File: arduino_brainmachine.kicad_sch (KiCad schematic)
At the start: 180 parts, among them Q1 2N5551, Q2 2N5551, Q3 2N5551, Q4 2N5551, Q5 BD139, Q6 BD139, Q8 2N5551, SW1 SW_Push, U1 TVS 05V, U2 TVS 05V, U3 LM358_DFN, U4 L7805_TO220, U5 TVS 12V, U6 TVS 12V, Y1 6.5 KHz or 2.5 kHz, Y2 6.5 KHz or 2.5 kHz, Y3 6.5 KHz or 2.5 kHz

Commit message: Upgrade
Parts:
- removed SW1: SW_Push, symbol Switch:SW_Push
- added C51, C52: 10-20, symbol Device:C_Small
- added D29, D30: D, symbol Device:D
- added D31, D32, D33, D34: LED, symbol Device:LED
- added Q7, Q9: 2N2222, Package_TO_SOT_THT:TO-39-3, symbol Transistor_BJT:2N2219
- added R60, R77: 10 KOm, symbol PCM_Elektuur:R
- added R61, R79: 100 KOm, symbol PCM_Elektuur:R
- added R75, R76, R78, R80, R81: 1 kOm, symbol PCM_Elektuur:R
- Q4, Q8: value 2N5551 -> 2N2222
- R21: value 220 Om -> 1 kOm
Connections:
- net +5V: now also R61.2 (-), R75.2 (-), R79.2 (-), R80.2 (-)
- net GND: now also C51.2, C52.2, D29.2 (A), D30.2 (A), D31.1 (K), D32.1 (K), D33.1 (K), D34.1 (K), Q7.1 (E), Q9.1 (E), R60.1 (+), R77.1 (+)
- net LED: now also A1.1 (D1/TX), A1.2 (D0/RX), R21.2 (-), R81.2 (-)
- net at D1.2 (A), D2.2 (A), R10.2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: now also D34.2 (A)
- net at D10.2 (A), D8.2 (A), R30.2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: now also D33.2 (A)
- net at R21.1 (+): now also D31.2 (A); no longer A1.5 (D2)
- net at D23.2 (A): now also C51.1, D29.1 (K), Q7.3 (C), R75.1 (+); no longer A1.10 (D7)
- net at A1.13 (D10): now also R76.2 (-); no longer D24.2 (A)
- new net: Q7.2 (B), R60.2 (-), R61.1 (+), R76.1 (+)
- new net: Q9.2 (B), R77.2 (-), R78.1 (+), R79.1 (+)
- new net: A1.10 (D7), R78.2 (-)
- new net: D32.2 (A), R81.1 (+)
- new net LEDPD: C52.1, D24.2 (A), D30.1 (K), Q9.3 (C), R80.1 (+)
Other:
- note removed: "Im dont use this switch and BrainWave Entertaiment program from spring"
- moved on the sheet: RV1, RV2, RV3, RV4

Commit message: Upgrade
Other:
- note added: "2025.09.03"
- note added: "Must be OSH"
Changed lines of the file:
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@@
 		(date "2025-02-18")
+	)
+	(text "2025.09.03"
+		(exclude_from_sim no)
+		(at 257.81 183.642 0)
+		(effects
+			(font
+				(size 1.27 1.27)
+			)
+		)
 	)
 	(text "Install all from first to bigger value"
@@
 		(effects
 			(font
+				(size 1.27 1.27)
+			)
+		)
+	)
+	(text "Must be OSH"
+		(exclude_from_sim no)
+		(at 254.508 177.8 0)
+		(effects
+			(font

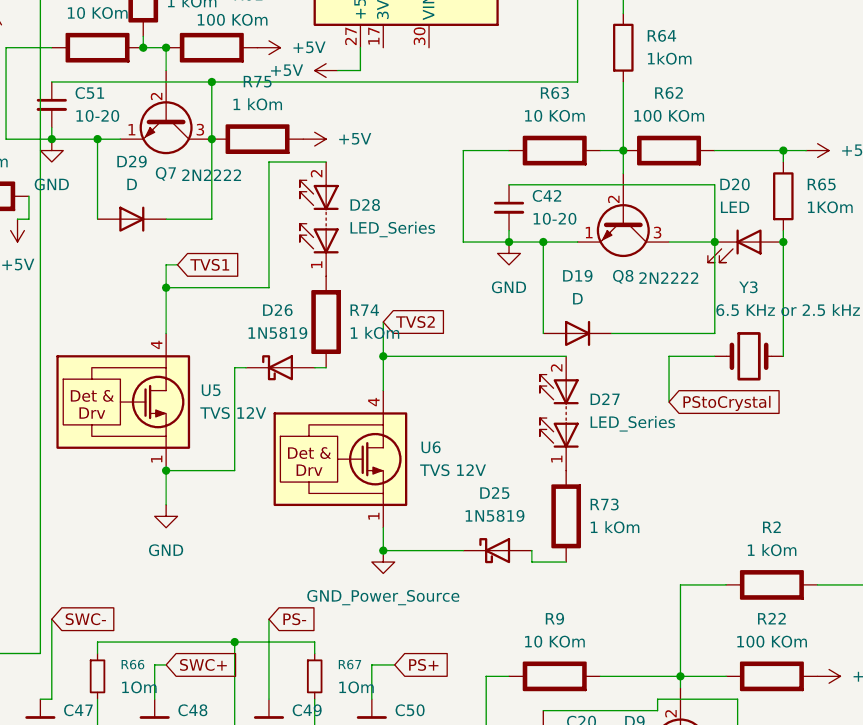
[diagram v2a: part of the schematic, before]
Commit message: Removed thing from piracy
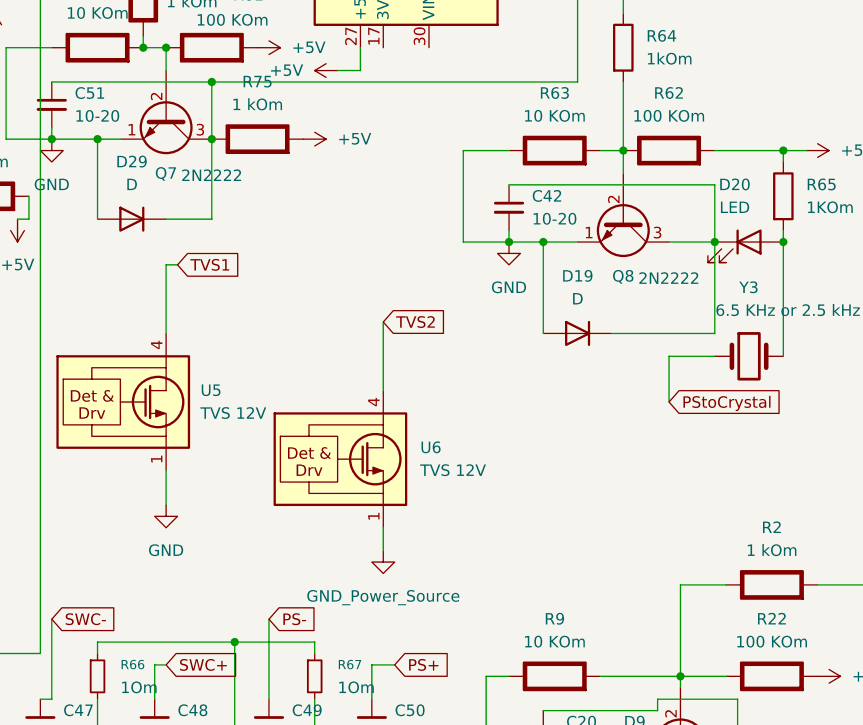
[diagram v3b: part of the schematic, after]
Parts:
- removed D25, D26: 1N5819, Diode_THT:D_DO-41_SOD81_P10.16mm_Horizontal, symbol Diode:1N5819
- removed D27, D28: LED_Series, symbol Device:LED_Series
- removed R73, R74: 1 kOm, symbol PCM_Elektuur:R

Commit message: Upgrade
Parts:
- removed C12, C14, C36, C37: 100nF, symbol PCM_Elektuur:C
- removed D23: LED, symbol Device:LED
- removed R59: 220 Om, symbol PCM_Elektuur:R
- removed R66, R67, R68, R69, R70: 1Om, symbol Device:R_Small
- added C12: 10-20, symbol Device:C_Small
- added D23: D, symbol Device:D
- added Q10: 2N2222, Package_TO_SOT_THT:TO-39-3, symbol Transistor_BJT:2N2219
- added Q11: BD139, Package_TO_SOT_THT:TO-39-3, symbol Transistor_BJT:2N2219
- added R59, R73, R74: 1KOm, symbol Device:R
- added U7, U8, U9: PC123, symbol Isolator:Optocoupler_DC_PhotoNPN_AKEC
- C19, C21, C24, C27, C39, C41: value 100pF-100nF -> 100pF-100nF and 100-1000nF
- D24: value LED -> 12v LED, 3-4 cm strip
- Q3: value 2N5551 -> 2N2222
- R37: value 220 Om -> 10 KOm
- R38: value 220 Om -> 100 KOm
- R58: value 220 Om -> 1 kOm
- renumbered C1 to C1?????, C2 to C2?????, C3 to C3????, C4 to C4?????
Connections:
- net +5V: now also R38.2 (-), U9.1
- net Earth_Protective: now also 12V.2 (A+), 5.1V.2 (A+), 5.1V1.2 (A+), A1.29 (GND), A1.4 (GND), C10.2 (-), C11.2 (-), C13.2 (-), C15.2 (-), C17.2 (-), C18.2 (-), C20.2, C23.2, C38.2 (-), C39.2, C40.2 (-), C41.2, C42.2, C43.1, C44.1, C45.1, C46.1, C47.2, C48.2, C49.2, C50.2, C51.2, C52.2, C7.2 (-), C9.2, D12.2 (A), D19.2 (A), D24.1 (K), D29.2 (A), D3.1 (K), D30.2 (A), D31.1 (K), D32.1 (K), D33.1 (K), D34.1 (K), D4.2 (A), D5.1 (K), D6.1 (K), D7.1 (K), D9.2 (A), MK1.1 (-), Q3.1 (E), Q4.1 (E), Q5.1 (E), Q7.1 (E), Q8.1 (E), Q9.1 (E), R14.1 (+), R15.1 (+), R19.1 (+), R20.1 (+), R25.2 (-), R29.2 (-), R37.1 (+), R4.1 (+), R43.1 (+), R60.1 (+), R63.1 (+), R77.1 (+), R9.1 (+), RV2.3, RV4.3, RV5.3, RV5.6, U1.1 (GND), U1.2 (GND), U1.3 (GND), U1.7 (GND), U2.1 (GND), U2.2 (GND), U2.3 (GND), U2.7 (GND), U4.2 (GND), U5.1 (GND), U5.2 (GND), U5.3 (GND), U5.7 (GND), C12.2, D23.2 (A), Q10.1 (E), U7.2, U8.2, U9.2, U9.3
- net GND_Power_Source: no longer R58.2 (-)
- net LEDPD: now also U8.1; no longer D24.2 (A)
- net SWC-: now also R73.1, R74.2
- net SWPS1: now also U8.3; no longer D24.1 (K)
- net SWPS2: now also U7.3
- net at R76.2 (-): now also A1.11 (D8); no longer A1.13 (D10)
- net at R8.1 (+): now also A1.12 (D9); no longer A1.11 (D8)
- net at C51.1, D29.1 (K), Q7.3 (C)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: now also U7.1
- net at R7.1 (+): now also A1.13 (D10); no longer A1.12 (D9)
- net at R58.1 (+): now also R37.2 (-), R38.1 (+), Q10.2 (B)
- net FHGND: now reaches A1.9 (D6)
- net FHGND: now also R58.2 (-)
- net 12v Power Source renamed +12V
- net +12V: now also Q11.3 (C), R59.1
- removed net GND: 12V.2 (A+), 5.1V.2 (A+), 5.1V1.2 (A+), A1.29 (GND), A1.4 (GND), C10.2 (-), C11.2 (-), C13.2 (-), C15.2 (-), C17.2 (-), C18.2 (-), C20.2, C23.2, C38.2 (-), C39.2, C40.2 (-), C41.2, C42.2, C51.2, C52.2, C7.2 (-), C9.2, D12.2 (A), D19.2 (A), D29.2 (A), D3.1 (K), D30.2 (A), D31.1 (K), D32.1 (K), D33.1 (K), D34.1 (K), D4.2 (A), D5.1 (K), D6.1 (K), D7.1 (K), D9.2 (A), MK1.1 (-), Q3.1 (E), Q4.1 (E), Q5.1 (E), Q7.1 (E), Q8.1 (E), Q9.1 (E), R14.1 (+), R15.1 (+), R19.1 (+), R20.1 (+), R25.2 (-), R29.2 (-), R37.2 (-), R38.2 (-), R4.1 (+), R43.1 (+), R60.1 (+), R63.1 (+), R77.1 (+), R9.1 (+), RV2.3, RV4.3, RV5.3, RV5.6, U1.1 (GND), U1.2 (GND), U1.3 (GND), U1.7 (GND), U2.1 (GND), U2.2 (GND), U2.3 (GND), U2.7 (GND), U4.2 (GND), U5.1 (GND), U5.2 (GND), U5.3 (GND), U5.7 (GND)
- new net: Q11.2 (B), R59.2, U9.4
- new net: D24.2 (A), Q11.1 (E)
- new net: R74.1, U8.4
- new net: R73.2, U7.4
- new net: C12.1, D23.1 (K), Q10.3 (C)
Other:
- note added: "2025. sping/start of summer, 2025.10.05"
- note added: "CapSet"
- moved on the sheet: R64, U5, U6

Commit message: fixed error
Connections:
- net Earth_Protective: no longer U9.3
- net at R59.2, U9.4: no longer Q11.2 (B)
- new net: Q11.2 (B), U9.3
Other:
- note added: "2025.10.05 - error fix"
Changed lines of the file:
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@@
 		)
 	)
+	(text "2025.10.05 - error fix"
+		(exclude_from_sim no)
+		(at 234.442 171.45 0)
+		(effects
+			(font
+				(size 1.27 1.27)
+			)
+		)
+	)
 	(text "Install all from first to bigger value"
 		(exclude_from_sim no)
@@
 	)
 	(junction
-		(at 128.27 135.89)
-		(diameter 0)
-		(color 0 0 0 0)
-	)
-	(junction
 		(at 24.13 67.31)
 		(diameter 0)
@@
 	)
 	(junction
-		(at 128.27 142.24)
-		(diameter 0)
-		(color 0 0 0 0)
-	)
-	(junction
 		(at 93.98 130.81)
 		(diameter 0)
@@
 	(wire
 		(pts
+			(xy 129.54 135.89) (xy 129.54 140.97)
+		)
+		(stroke
+			(width 0)
+			(type default)
+		)
+	)
+	(wire
+		(pts
 			(xy 29.21 46.99) (xy 38.1 46.99)
 		)
@@
 	(wire
 		(pts
-			(xy 128.27 140.97) (xy 128.27 142.24)
-		)
-		(stroke
-			(width 0)
-			(type default)
-		)
-	)
-	(wire
-		(pts
 			(xy 25.4 66.04) (xy 25.4 67.31)
 		)
@@
 	(wire
 		(pts
+			(xy 128.27 140.97) (xy 129.54 140.97)
+		)
+		(stroke
+			(width 0)
+			(type default)
+		)
+	)
+	(wire
+		(pts
 			(xy 119.38 191.77) (xy 125.73 191.77)
 		)
@@
 		)
 		(stroke
-			(width 0)
-			(type default)
-		)
-	)
-	(wire
-		(pts
-			(xy 128.27 135.89) (xy 129.54 135.89)
-		)
-		(stroke

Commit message: Upgrdae
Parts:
- added 12V2, 12V3, 3.3v: ${SIM.PARAMS}, symbol PCM_Elektuur:D-Zener
- added U10: TVS 3.3V, Package_SON:WSON-6-1EP_2x2mm_P0.65mm_EP1x1.6mm, symbol Power_Protection:TVS0500DRV
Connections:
- net Earth_Protective: now also 3.3v.2 (A+), U10.1 (GND), U10.2 (GND), U10.3 (GND), U10.7 (GND)
- net GND_Power_Source: now also 12V2.1 (K-)
- net SWC-: now also 12V3.1 (K-)
- net at C25.2 (-), C26.1, C27.2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: now also 12V2.2 (A+)
- net at C22.2 (-), C23.1, C24.2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: now also 12V3.2 (A+)
- new net +3.3V: 3.3v.1 (K-), U10.4 (IN), U10.5 (IN), U10.6 (IN)
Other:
- moved on the sheet: U2

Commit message: Updated
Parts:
- added 12V4, 12V5: ${SIM.PARAMS}, symbol PCM_Elektuur:D-Zener
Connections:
- net +12V: now also 12V2.2 (A+)
- net Earth_Protective: now also 12V3.2 (A+)
- net GND_Power_Source: now also 12V5.2 (A+); no longer 12V2.1 (K-)
- net SWC-: now also 12V4.2 (A+); no longer 12V3.1 (K-)
- net at C25.2 (-), C26.1, C27.2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: no longer 12V2.2 (A+)
- net at C22.2 (-), C23.1, C24.2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: no longer 12V3.2 (A+)
- new net: 12V2.1 (K-), 12V5.1 (K-)
- new net: 12V3.1 (K-), 12V4.1 (K-)
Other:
- moved on the sheet: 12V1, 12V3

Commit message: update
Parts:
- added 5.1V2, 5.1V3: ${SIM.PARAMS}, symbol PCM_Elektuur:D-Zener
- added D25: ESD9B3.3ST5G, Diode_SMD:D_SOD-923, symbol Diode:ESD9B3.3ST5G
- added D26: D, symbol Device:D
- added U11: LD1117V33, Package_TO_SOT_THT:TO-220-3_Vertical, symbol Regulator_Linear:LD1117V33
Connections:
- net CapSet is gone; now on net First SW capacitor set: C40.1 (+), C41.1
- net TVS is gone; now on net First SW capacitor set: 5.1V.1 (K-), C10.1 (+), C18.1 (+), C7.1 (+), D11.2 (A), L1.2 (-), R39.2 (-), U2.4 (IN), U2.5 (IN), U2.6 (IN), U4.3 (VO)
- net +3.3V: now also A1.17 (3V3), D25.2 (A2), D26.2 (A), U11.2 (VO)
- net +5V: now also 5.1V3.2 (A+), D26.1 (K), U11.3 (VI)
- net Earth_Protective: now also 5.1V2.2 (A+), D25.1 (A1), U11.1 (GND)
- new net: 5.1V2.1 (K-), 5.1V3.1 (K-)
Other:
- moved on the sheet: C40, C41, D31, R21, R34, R81
